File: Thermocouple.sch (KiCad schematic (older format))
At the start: 0 parts

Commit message: Defining Your Inputs and Outputs
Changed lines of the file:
@@
 $EndDescr
 Text HLabel 9750 2000 2    60   Input ~ 0
-TC_IN_+
+TC_IN+
 Text HLabel 9750 2700 2    60   Input ~ 0
-TC_IN_-
+TC_IN-
+Text HLabel 1800 1900 0    60   Input ~ 0
+MOSI
+Text HLabel 1800 2100 0    60   Output ~ 0
+MISO
+Text HLabel 1800 2300 0    60   Input ~ 0
+SCLK
+Text HLabel 1800 2500 0    60   Input ~ 0
+CS_N
 $EndSCHEMATC

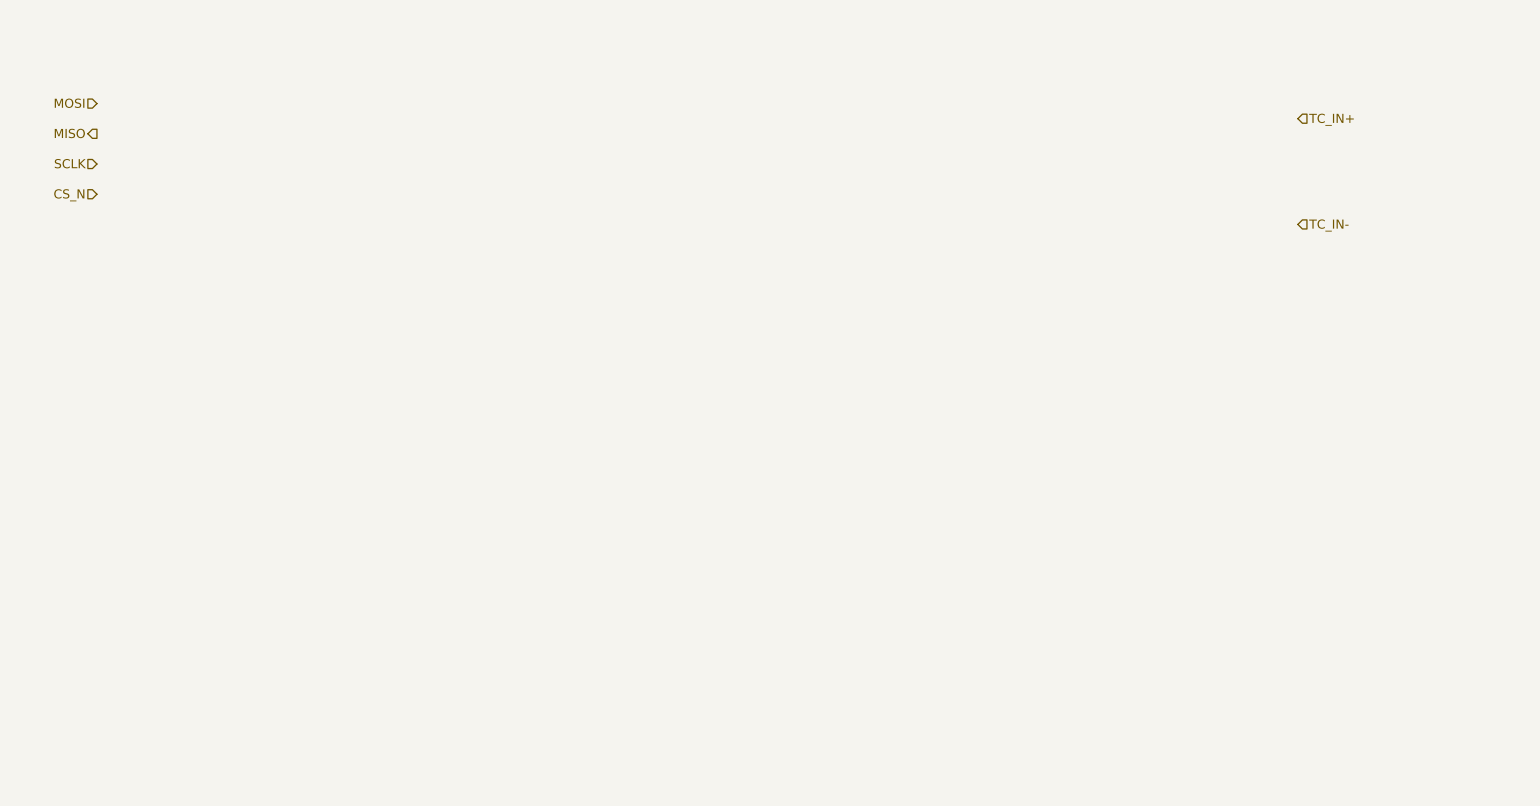
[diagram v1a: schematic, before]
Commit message: Understanding the Thermocouple Module
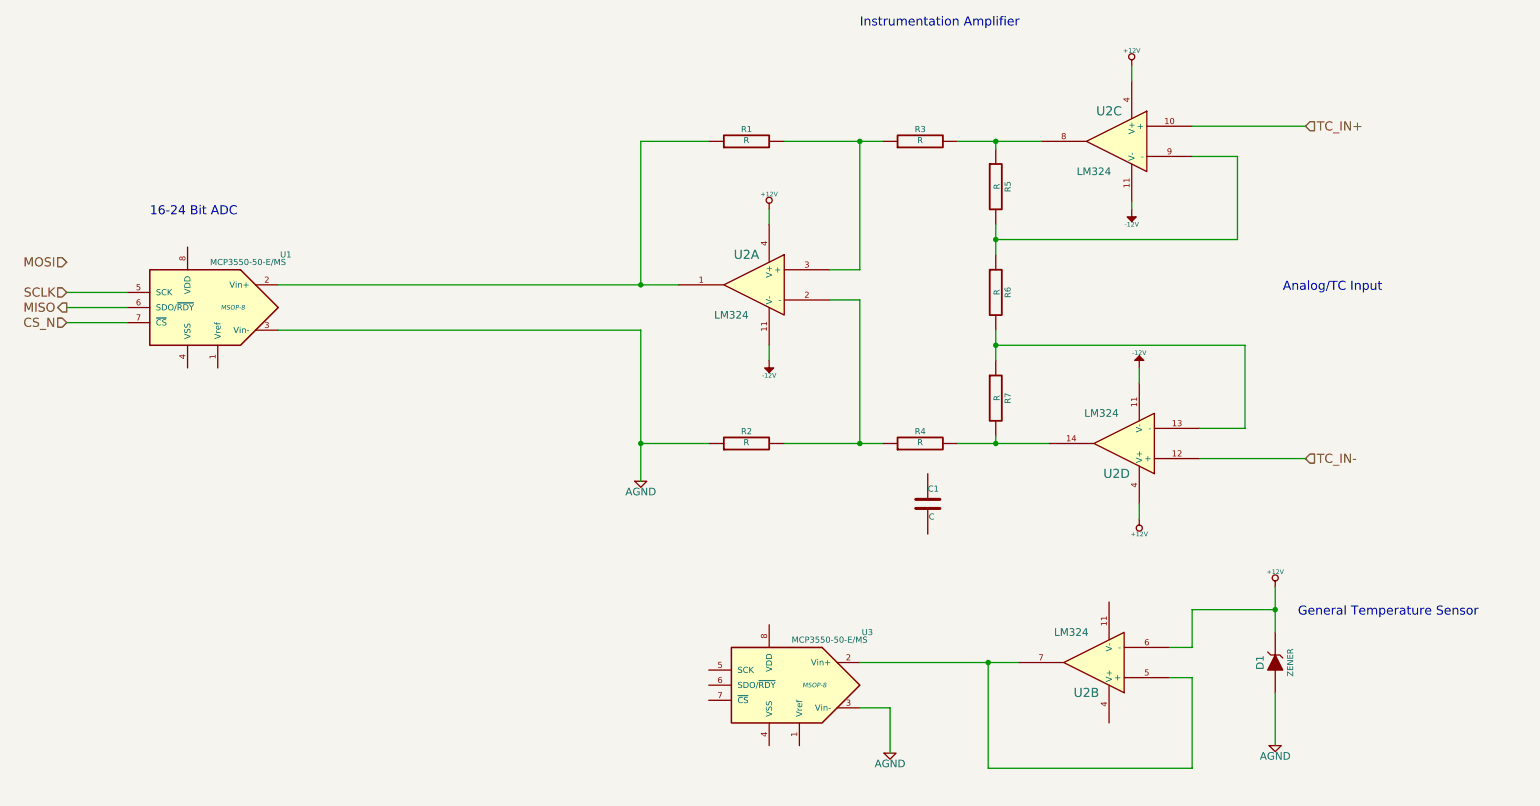
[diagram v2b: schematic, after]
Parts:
- added C1: C, symbol C
- added D1: ZENER, symbol ZENER
- added R1, R2, R3, R4, R5, R6, R7: R, symbol R
- added U1, U3: MCP3550-50-E/MS, MSOP-8, symbol MCP3550-50-E/MS
- added U2: LM324, symbol LM324
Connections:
- net CS_N: now also U1.7 (~CS~)
- net MISO: now also U1.6 (SDO/~RDY~)
- net SCLK: now also U1.5 (SCK)
- net TC_IN+: now also U2.10 (+)
- net TC_IN-: now also U2.12 (+)
- new net: R3.2, R5.1, U2.8
- new net: R5.2, R6.1, U2.9 (-)
- new net: R6.2, R7.1, U2.13 (-)
- new net: R4.2, R7.2, U2.14
- new net: R1.1, U1.2 (Vin+), U2.1
- new net: R2.2, R4.1, U2.2 (-)
- new net: R1.2, R3.1, U2.3 (+)
- new net: U2.5 (+), U2.7, U3.2 (Vin+)
- new net +12V: D1.2 (K), U2.4 (V+), U2.4 (V+), U2.4 (V+), U2.6 (-)
- new net -12V: U2.11 (V-), U2.11 (V-), U2.11 (V-)
- new net AGND: D1.1 (A), R2.1, U1.3 (Vin-), U3.3 (Vin-)
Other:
- note added: "16-24 Bit ADC"
- note added: "Analog/TC Input"
- note added: "General Temperature Sensor"
- note added: "Instrumentation Amplifier"

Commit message: Understanding the Arduino Module
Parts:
- renumbered U2 to U?
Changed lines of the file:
@@
 LIBS:valves
 LIBS:MyComponents
+LIBS:arduino_shieldsNCL
 LIBS:BenchBuddy-cache
 EELAYER 24 0
@@
 CS_N
 $Comp
-L LM324 U2
+L LM324 U?
 U 3 1 52F04340
 P 8550 2150
-F 0 "U2" H 8600 2350 60  0000 C CNN
+F 0 "U?" H 8600 2350 60  0000 C CNN
 F 1 "LM324" H 8700 1950 50  0000 C CNN
 F 2 "" H 8550 2150 60  0000 C CNN
@@
 $EndComp
 $Comp
-L LM324 U2
+L LM324 U?
 U 4 1 52F0436B
 P 8600 4150
-F 0 "U2" H 8650 4350 60  0000 C CNN
+F 0 "U?" H 8650 4350 60  0000 C CNN
 F 1 "LM324" H 8750 3950 50  0000 C CNN
 F 2 "" H 8600 4150 60  0000 C CNN
@@
 $EndComp
 $Comp
-L LM324 U2
+L LM324 U?
 U 1 1 52F043FC
 P 6150 3100
-F 0 "U2" H 6200 3300 60  0000 C CNN
+F 0 "U?" H 6200 3300 60  0000 C CNN
 F 1 "LM324" H 6300 2900 50  0000 C CNN
 F 2 "" H 6150 3100 60  0000 C CNN
@@
 $EndComp
 $Comp
-L LM324 U2
+L LM324 U?
 U 2 1 52F0446F
 P 8400 5600
-F 0 "U2" H 8450 5800 60  0000 C CNN
+F 0 "U?" H 8450 5800 60  0000 C CNN
 F 1 "LM324" H 8550 5400 50  0000 C CNN
 F 2 "" H 8400 5600 60  0000 C CNN

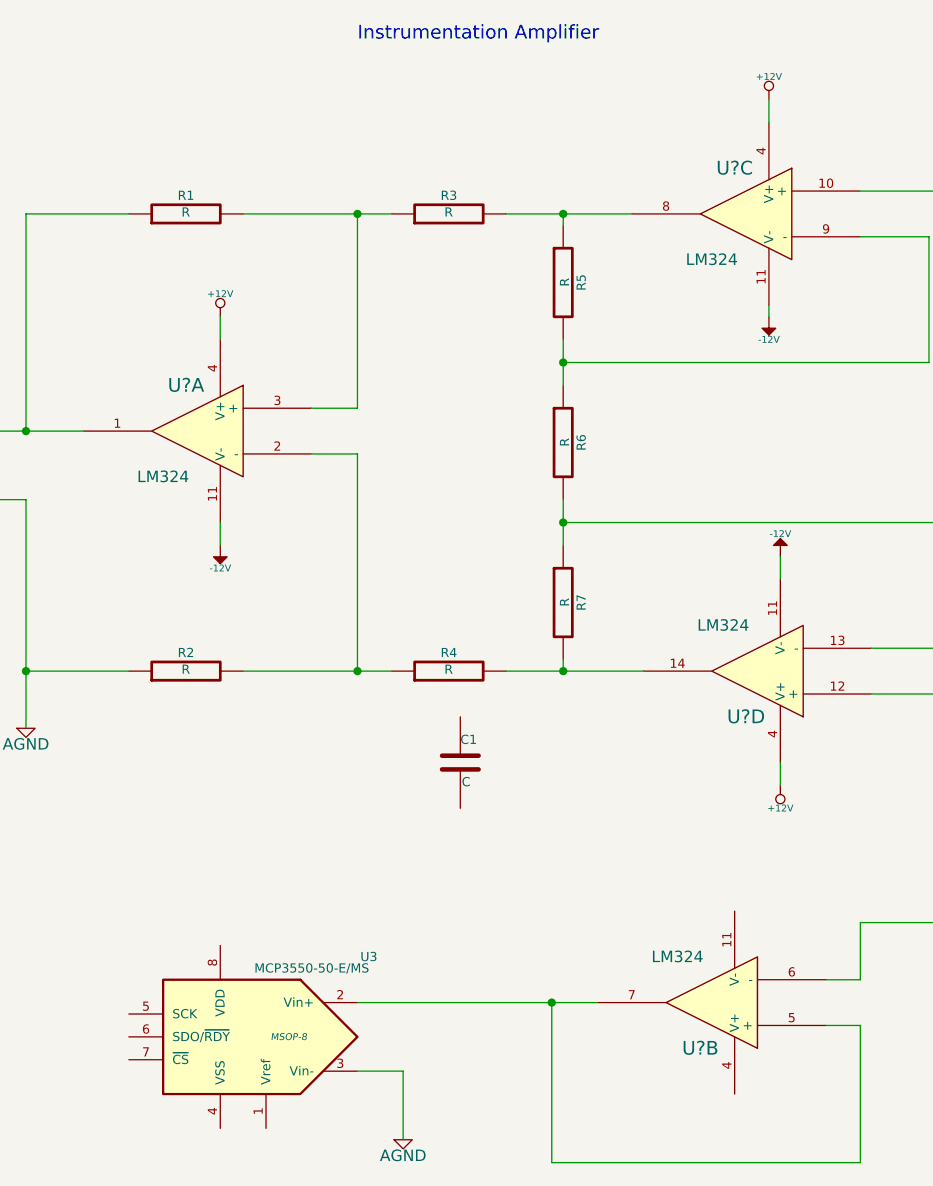
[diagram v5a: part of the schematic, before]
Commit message: Associating and Placing the Relay Module
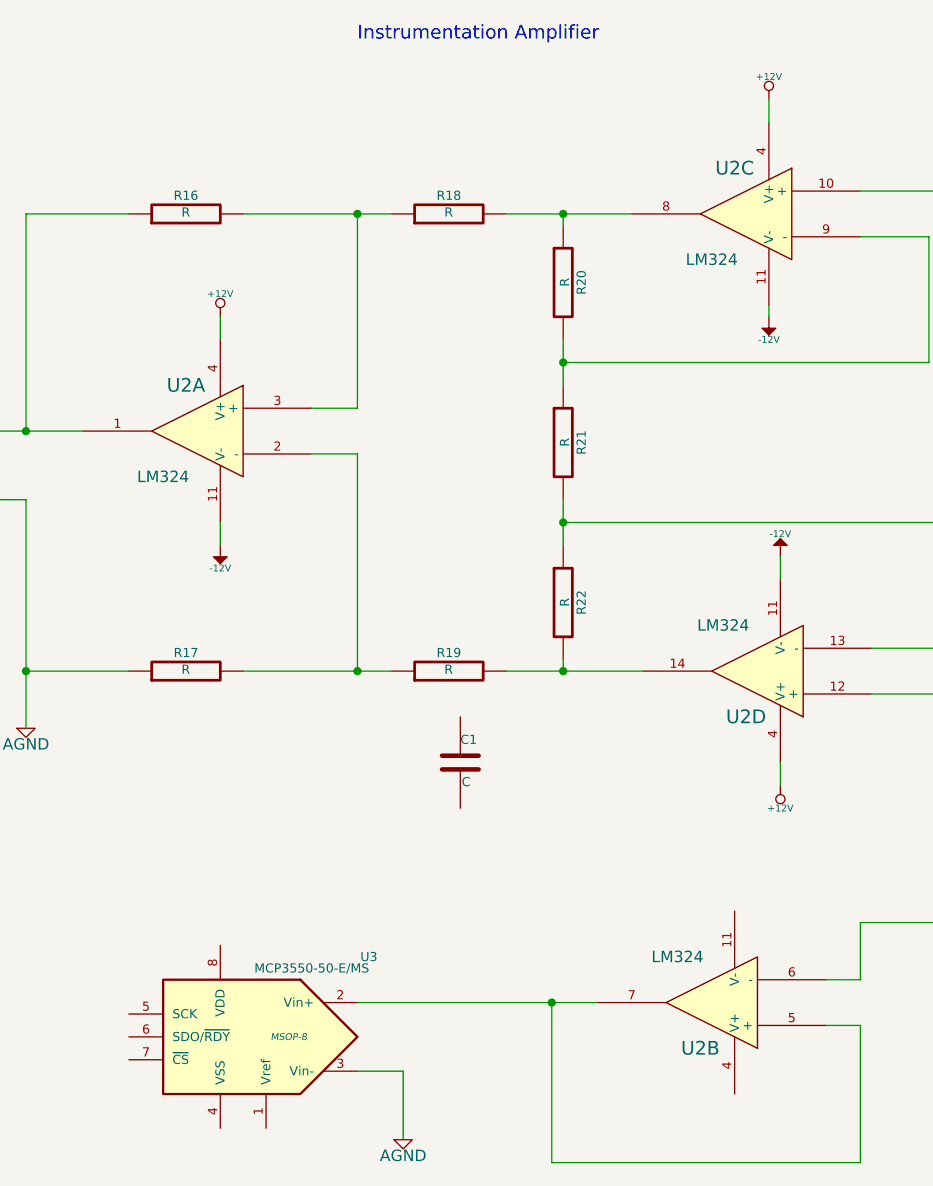
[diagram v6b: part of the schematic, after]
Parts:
- gave numbers to parts that had none: 1
- renumbered R1 to R16, R2 to R17, R3 to R18, R4 to R19, R5 to R20, R6 to R21, R7 to R22
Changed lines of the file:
@@
 CS_N
 $Comp
-L LM324 U?
+L LM324 U2
 U 3 1 52F04340
 P 8550 2150
-F 0 "U?" H 8600 2350 60  0000 C CNN
+F 0 "U2" H 8600 2350 60  0000 C CNN
 F 1 "LM324" H 8700 1950 50  0000 C CNN
 F 2 "" H 8550 2150 60  0000 C CNN
@@
 $EndComp
 $Comp
-L LM324 U?
+L LM324 U2
 U 4 1 52F0436B
 P 8600 4150
-F 0 "U?" H 8650 4350 60  0000 C CNN
+F 0 "U2" H 8650 4350 60  0000 C CNN
 F 1 "LM324" H 8750 3950 50  0000 C CNN
 F 2 "" H 8600 4150 60  0000 C CNN
@@
 $EndComp
 $Comp
-L R R5
+L R R20
 U 1 1 52F0439A
 P 7750 2450
-F 0 "R5" V 7830 2450 40  0000 C CNN
+F 0 "R20" V 7830 2450 40  0000 C CNN
 F 1 "R" V 7757 2451 40  0000 C CNN
 F 2 "" V 7680 2450 30  0000 C CNN
@@
 $EndComp
 $Comp
-L R R6
+L R R21
 U 1 1 52F043AC
 P 7750 3150
-F 0 "R6" V 7830 3150 40  0000 C CNN
+F 0 "R21" V 7830 3150 40  0000 C CNN
 F 1 "R" V 7757 3151 40  0000 C CNN
 F 2 "" V 7680 3150 30  0000 C CNN
@@
 $EndComp
 $Comp
-L R R7
+L R R22
 U 1 1 52F043B7
 P 7750 3850
-F 0 "R7" V 7830 3850 40  0000 C CNN
+F 0 "R22" V 7830 3850 40  0000 C CNN
 F 1 "R" V 7757 3851 40  0000 C CNN
 F 2 "" V 7680 3850 30  0000 C CNN
@@
 $EndComp
 $Comp
-L LM324 U?
+L LM324 U2
 U 1 1 52F043FC
 P 6150 3100
-F 0 "U?" H 6200 3300 60  0000 C CNN
+F 0 "U2" H 6200 3300 60  0000 C CNN
 F 1 "LM324" H 6300 2900 50  0000 C CNN
 F 2 "" H 6150 3100 60  0000 C CNN
@@
 $EndComp
 $Comp
-L R R3
+L R R18
 U 1 1 52F04434
 P 7250 2150
-F 0 "R3" V 7330 2150 40  0000 C CNN
+F 0 "R18" V 7330 2150 40  0000 C CNN
 F 1 "R" V 7257 2151 40  0000 C CNN
 F 2 "" V 7180 2150 30  0000 C CNN
@@
 $EndComp
 $Comp
-L R R1
+L R R16
 U 1 1 52F0443F
 P 6100 2150
-F 0 "R1" V 6180 2150 40  0000 C CNN
+F 0 "R16" V 6180 2150 40  0000 C CNN
 F 1 "R" V 6107 2151 40  0000 C CNN
 F 2 "" V 6030 2150 30  0000 C CNN
@@
 $EndComp
 $Comp
-L R R4
+L R R19
 U 1 1 52F0444A
 P 7250 4150
-F 0 "R4" V 7330 4150 40  0000 C CNN
+F 0 "R19" V 7330 4150 40  0000 C CNN
 F 1 "R" V 7257 4151 40  0000 C CNN
 F 2 "" V 7180 4150 30  0000 C CNN
@@
 $EndComp
 $Comp
-L R R2
+L R R17
 U 1 1 52F0445A
 P 6100 4150
-F 0 "R2" V 6180 4150 40  0000 C CNN
+F 0 "R17" V 6180 4150 40  0000 C CNN
 F 1 "R" V 6107 4151 40  0000 C CNN
 F 2 "" V 6030 4150 30  0000 C CNN
@@
 $EndComp
 $Comp
-L LM324 U?
+L LM324 U2
 U 2 1 52F0446F
 P 8400 5600
-F 0 "U?" H 8450 5800 60  0000 C CNN
+F 0 "U2" H 8450 5800 60  0000 C CNN
 F 1 "LM324" H 8550 5400 50  0000 C CNN
 F 2 "" H 8400 5600 60  0000 C CNN
@@
 $EndComp
 $Comp
-L -12V #PWR6
+L -12V #PWR03
 U 1 1 52F04584
 P 8650 2600
-F 0 "#PWR6" H 8650 2730 20  0001 C CNN
+F 0 "#PWR03" H 8650 2730 20  0001 C CNN
 F 1 "-12V" H 8650 2700 30  0000 C CNN
 F 2 "" H 8650 2600 60  0000 C CNN
@@
 $EndComp
 $Comp
-L +12V #PWR5
+L +12V #PWR04
 U 1 1 52F045EB
 P 8650 1650
-F 0 "#PWR5" H 8650 1600 20  0001 C CNN
+F 0 "#PWR04" H 8650 1600 20  0001 C CNN
 F 1 "+12V" H 8650 1750 30  0000 C CNN
 F 2 "" H 8650 1650 60  0000 C CNN
@@
 $EndComp
 $Comp
-L +12V #PWR8
+L +12V #PWR05
 U 1 1 52F04627
 P 8700 4650
-F 0 "#PWR8" H 8700 4600 20  0001 C CNN
+F 0 "#PWR05" H 8700 4600 20  0001 C CNN
 F 1 "+12V" H 8700 4750 30  0000 C CNN
 F 2 "" H 8700 4650 60  0000 C CNN
@@
 $EndComp
 $Comp
-L +12V #PWR2
+L +12V #PWR06
 U 1 1 52F04632
 P 6250 2600
-F 0 "#PWR2" H 6250 2550 20  0001 C CNN
+F 0 "#PWR06" H 6250 2550 20  0001 C CNN
 F 1 "+12V" H 6250 2700 30  0000 C CNN
 F 2 "" H 6250 2600 60  0000 C CNN
@@
 $EndComp
 $Comp
-L -12V #PWR7
+L -12V #PWR07
 U 1 1 52F0463D
 P 8700 3650
-F 0 "#PWR7" H 8700 3780 20  0001 C CNN
+F 0 "#PWR07" H 8700 3780 20  0001 C CNN
 F 1 "-12V" H 8700 3750 30  0000 C CNN
 F 2 "" H 8700 3650 60  0000 C CNN
@@
 $EndComp
 $Comp
-L -12V #PWR3
+L -12V #PWR08
 U 1 1 52F04648
 P 6250 3600
-F 0 "#PWR3" H 6250 3730 20  0001 C CNN
+F 0 "#PWR08" H 6250 3730 20  0001 C CNN
 F 1 "-12V" H 6250 3700 30  0000 C CNN
 F 2 "" H 6250 3600 60  0000 C CNN
@@
 $EndComp
 $Comp
-L AGND #PWR1
+L AGND #PWR09
 U 1 1 52F04781
 P 5400 4400
-F 0 "#PWR1" H 5400 4400 40  0001 C CNN
+F 0 "#PWR09" H 5400 4400 40  0001 C CNN
 F 1 "AGND" H 5400 4330 50  0000 C CNN
 F 2 "" H 5400 4400 60  0000 C CNN
@@
 $EndComp
 $Comp
-L AGND #PWR10
+L AGND #PWR010
 U 1 1 52F049E8
 P 9600 6150
-F 0 "#PWR10" H 9600 6150 40  0001 C CNN
+F 0 "#PWR010" H 9600 6150 40  0001 C CNN
 F 1 "AGND" H 9600 6080 50  0000 C CNN
 F 2 "" H 9600 6150 60  0000 C CNN
@@
 $EndComp
 $Comp
-L +12V #PWR9
+L +12V #PWR011
 U 1 1 52F049F3
 P 9600 5100
-F 0 "#PWR9" H 9600 5050 20  0001 C CNN
+F 0 "#PWR011" H 9600 5050 20  0001 C CNN
 F 1 "+12V" H 9600 5200 30  0000 C CNN
 F 2 "" H 9600 5100 60  0000 C CNN
@@
 Connection ~ 7700 5600
 $Comp
-L AGND #PWR4
+L AGND #PWR012
 U 1 1 52F04BD3
 P 7050 6200
-F 0 "#PWR4" H 7050 6200 40  0001 C CNN
+F 0 "#PWR012" H 7050 6200 40  0001 C CNN
 F 1 "AGND" H 7050 6130 50  0000 C CNN
 F 2 "" H 7050 6200 60  0000 C CNN
